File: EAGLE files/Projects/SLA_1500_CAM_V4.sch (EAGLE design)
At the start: 88 parts, among them J2 JST GH SM06B, J3 MOLEX 53261-03, J4 MOLEX 53261-04, J5 MOLEX 53261-04, J6 MOLEX 53261-04, U11 TXS0102, U2 TPS73633DCQR, U8 TXS0102, U9 TXS0102

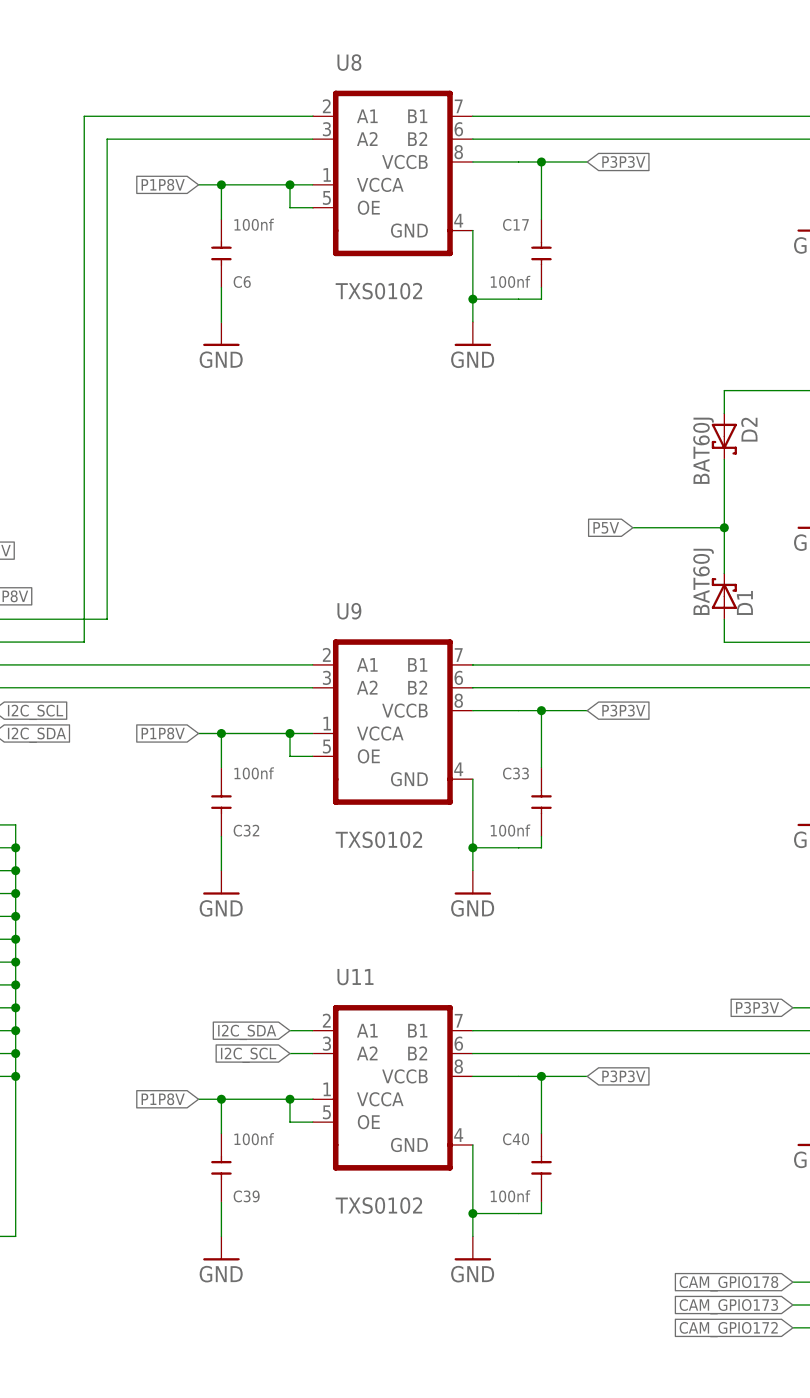
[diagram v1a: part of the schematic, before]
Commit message: Update SLA1500 CAM V4
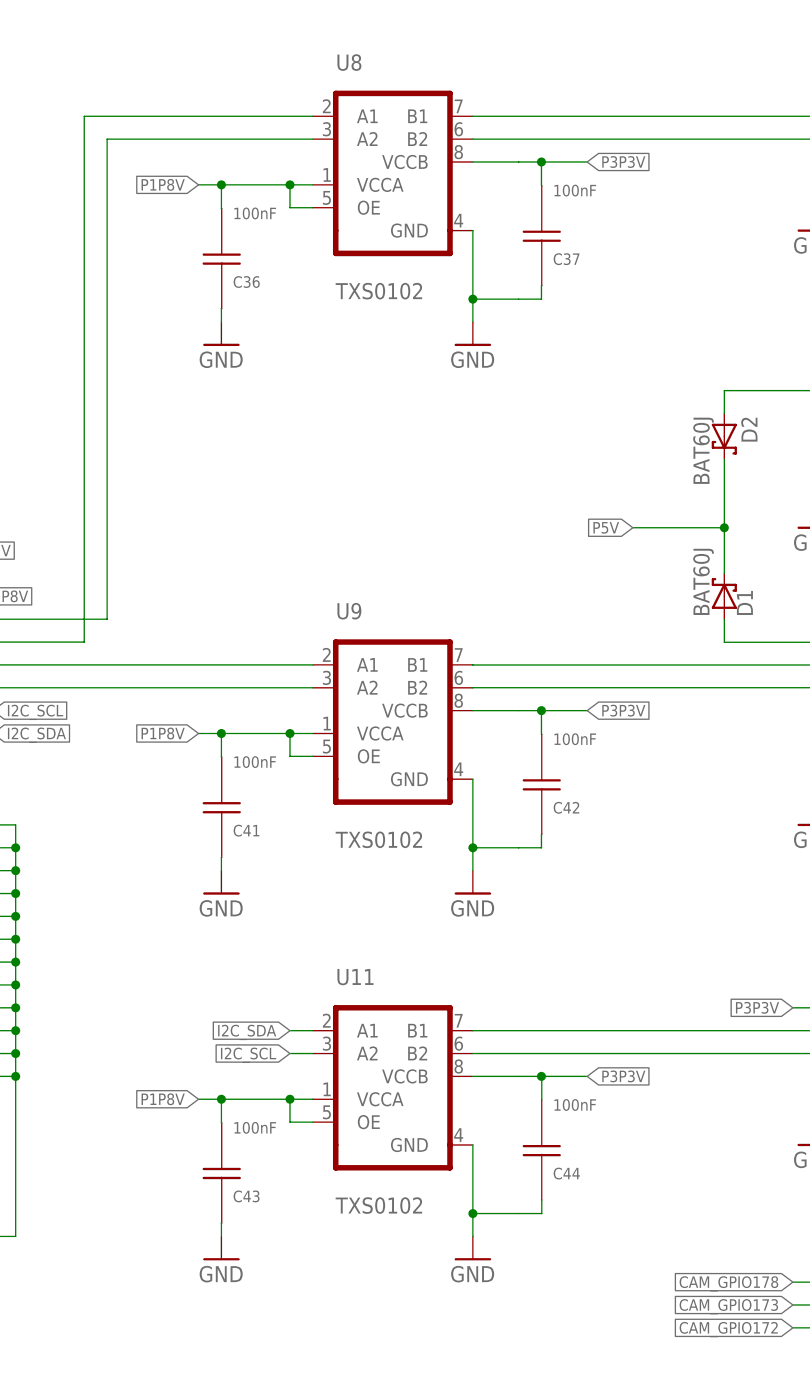
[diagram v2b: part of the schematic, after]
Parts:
- removed C17, C32, C33, C39, C40, C6: 100nf, Seeed-Capacitor:CERAMIC-100NF-25V-10%-X7R(0402)
- added C36, C37, C41, C42, C43, C44: (no value), Sightline:CAP0201100NF
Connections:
- net GND: now also C36.P$2, C37.P$2, C41.P$2, C42.P$2, C43.P$2, C44.P$2; no longer C17.2, C32.1, C33.2, C39.1, C40.2, C6.1
- net P1P8V: now also C36.P$1, C41.P$1, C43.P$1; no longer C32.2, C39.2, C6.2
- net P3P3V: now also C37.P$1, C42.P$1, C44.P$1; no longer C17.1, C33.1, C40.1

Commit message: Update SLA1500 CAM V4 .brd
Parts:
- added R17, R21, R22, R23, R24, R25, R3, R4, R5: 22R, Seeed-Resistor:SMD-RES-22R-1%-1/16W(0402)
- R15, R6: value 33R -> 22R; device Sightline:YC124-JR-0733RL -> Seeed-Resistor:SMD-RES-22R-1%-1/16W(0402)
- R7: value (none) -> 22R; device Sightline:YC124-JR-0733RL -> Seeed-Resistor:SMD-RES-22R-1%-1/16W(0402)
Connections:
- removed net N$10 (its old number): R6.4, U1.D_OUT(3)
- removed net N$50: R15.4, U1.D_OUT(11)
- removed net N$51: J1.CAM_D11, R15.5
- new net N$12: R15.1, U1.D_OUT(5)
- new net N$2: R3.1, U1.D_OUT(0)
- new net N$3: J1.CAM_D0, R3.2
- net N$11: now also J1.CAM_D4, R7.2; no longer J1.CAM_D3, R6.5
- net N$14: now also J1.CAM_D5, R15.2; no longer J1.CAM_D4, R7.8
- net N$22: now also R17.1, U1.D_OUT(6); no longer R7.2, U1.D_OUT(5)
- net N$24: now also J1.CAM_D6, R17.2; no longer J1.CAM_D5, R7.7
- net N$4: now also R4.1, U1.D_OUT(1); no longer R6.1, U1.D_OUT(0)
- net N$40: now also R21.1, U1.D_OUT(7); no longer R7.3, U1.D_OUT(6)
- net N$41: now also J1.CAM_D7, R21.2; no longer J1.CAM_D6, R7.6
- net N$42: now also R22.1, U1.D_OUT(8); no longer R7.4, U1.D_OUT(7)
- net N$43: now also J1.CAM_D8, R22.2; no longer J1.CAM_D7, R7.5
- net N$44: now also R23.1, U1.D_OUT(9); no longer R15.1, U1.D_OUT(8)
- net N$45: now also J1.CAM_D9, R23.2; no longer J1.CAM_D8, R15.8
- net N$46: now also R24.1, U1.D_OUT(10); no longer R15.2, U1.D_OUT(9)
- net N$47: now also J1.CAM_D10, R24.2; no longer J1.CAM_D9, R15.7
- net N$48: now also R25.1, U1.D_OUT(11); no longer R15.3, U1.D_OUT(10)
- net N$49: now also J1.CAM_D11, R25.2; no longer J1.CAM_D10, R15.6
- net N$5: now also J1.CAM_D1, R4.2; no longer J1.CAM_D0, R6.8
- net N$6: now also R5.1, U1.D_OUT(2); no longer R6.2, U1.D_OUT(1)
- net N$7: now also J1.CAM_D2, R5.2; no longer J1.CAM_D1, R6.7
- net N$8: now also R6.1, U1.D_OUT(3); no longer R6.3, U1.D_OUT(2)
- net N$9: now also J1.CAM_D3, R6.2; no longer J1.CAM_D2, R6.6

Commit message: Update SLA1500 CAM V4 .brd
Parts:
- removed R25: 22R, Seeed-Resistor:SMD-RES-22R-1%-1/16W(0402)
- removed U2: TPS73633DCQR, Sightline:TPS73633DCQR
- added R26: 33R, resistor:R-US_R0201
- added U10: TPS73633DBVR, Sightline:TPS73633DBVR
- R15, R17, R21, R22, R23, R24, R3, R4, R5, R6, R7: value 22R -> 33R; device Seeed-Resistor:SMD-RES-22R-1%-1/16W(0402) -> resistor:R-US_R0201
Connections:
- net GND: now also U10.GND; no longer U2.GND0, U2.GND1
- net N$10: now also R6.1; no longer R7.1
- net N$11: now also R6.2; no longer R7.2
- net N$12: now also R7.1; no longer R15.1
- net N$14: now also R7.2; no longer R15.2
- net N$2: now also R26.1; no longer R3.1
- net N$21: now also U10.NR; no longer U2.NR
- net N$22: now also R15.1; no longer R17.1
- net N$24: now also R15.2; no longer R17.2
- net N$3: now also R26.2; no longer R3.2
- net N$4: now also R3.1; no longer R4.1
- net N$40: now also R17.1; no longer R21.1
- net N$41: now also R17.2; no longer R21.2
- net N$42: now also R21.1; no longer R22.1
- net N$43: now also R21.2; no longer R22.2
- net N$44: now also R22.1; no longer R23.1
- net N$45: now also R22.2; no longer R23.2
- net N$46: now also R23.1; no longer R24.1
- net N$47: now also R23.2; no longer R24.2
- net N$48: now also R24.1; no longer R25.1
- net N$49: now also R24.2; no longer R25.2
- net N$5: now also R3.2; no longer R4.2
- net N$6: now also R4.1; no longer R5.1
- net N$7: now also R4.2; no longer R5.2
- net N$8: now also R5.1; no longer R6.1
- net N$9: now also R5.2; no longer R6.2
- net P3P3V: now also U10.OUT; no longer U2.OUT
- net P5V: now also U10.EN, U10.IN; no longer U2.EN, U2.IN
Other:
- moved on the sheet: C22, C23, C24
